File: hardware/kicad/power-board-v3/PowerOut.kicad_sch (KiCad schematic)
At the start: 10 parts, among them J1 3.3V LoRaWAN, J2 3.3V SWARM, J4 5V, J6 12V

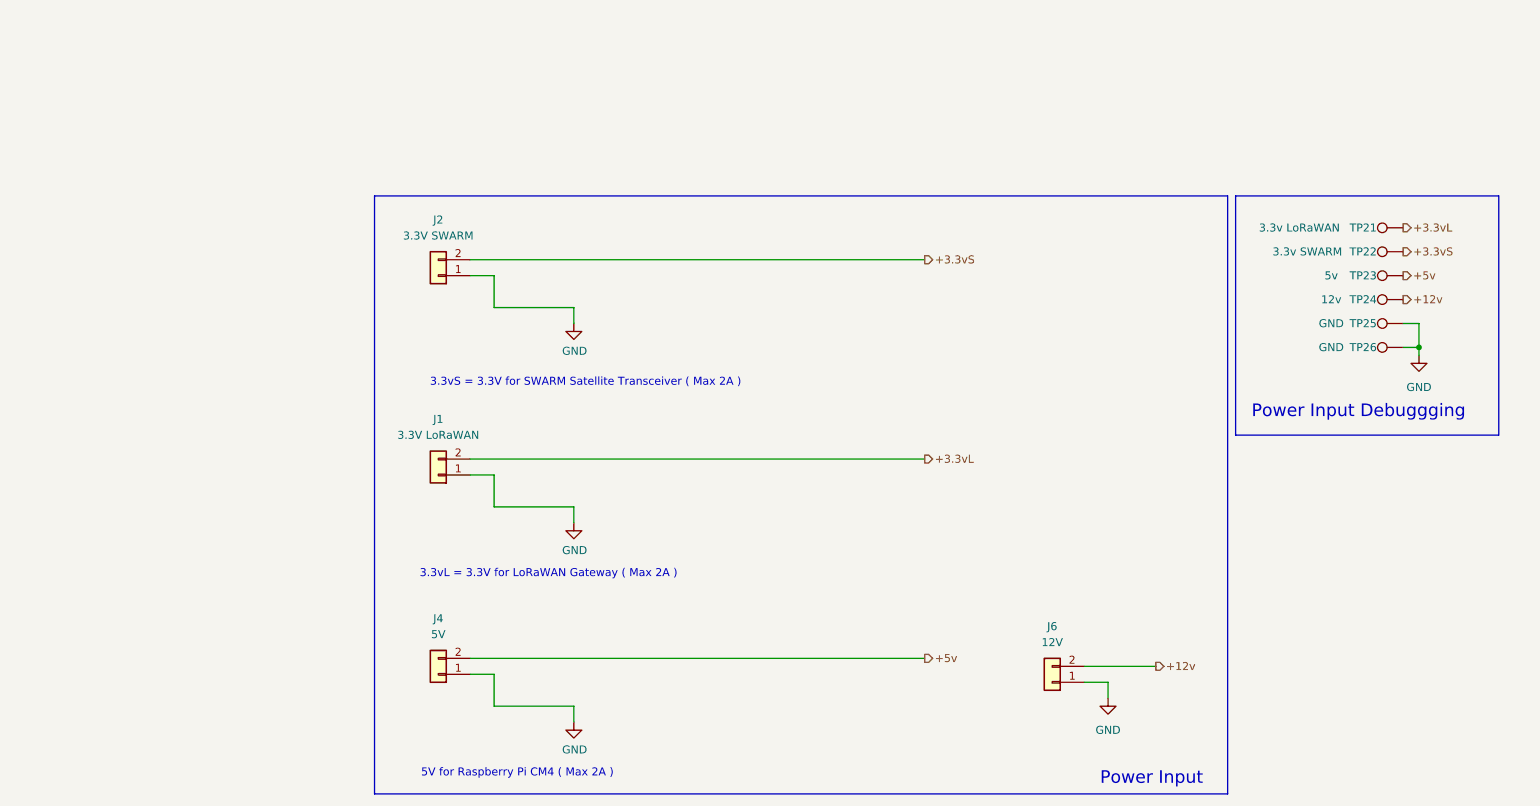
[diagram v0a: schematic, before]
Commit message: add power balance and regulator
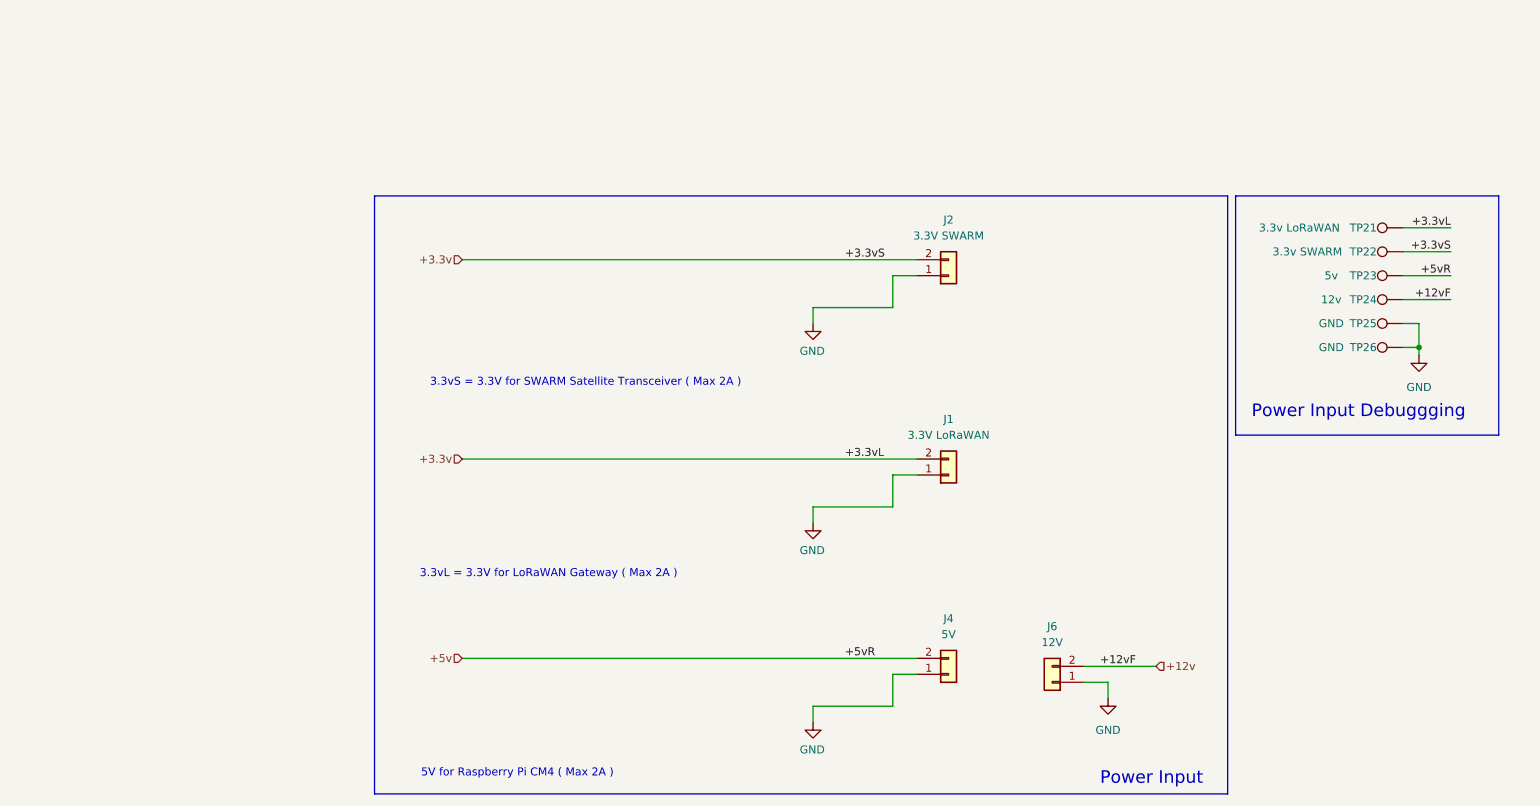
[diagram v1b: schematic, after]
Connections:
- net +3.3vS is gone; now on net +3.3v: J2.2 (Pin_2), TP22.1
- net +3.3vL renamed +3.3v
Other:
- moved on the sheet: J1, J2, J4

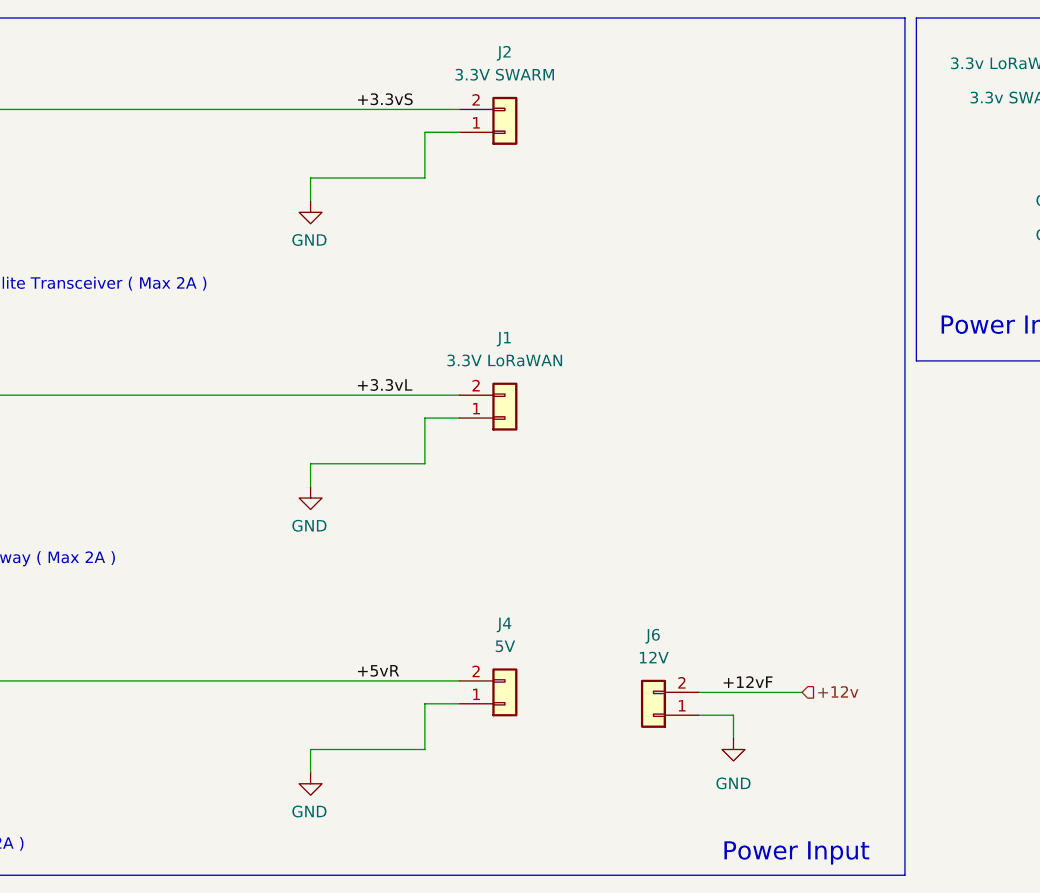
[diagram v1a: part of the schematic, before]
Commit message: add base symbol and wiring
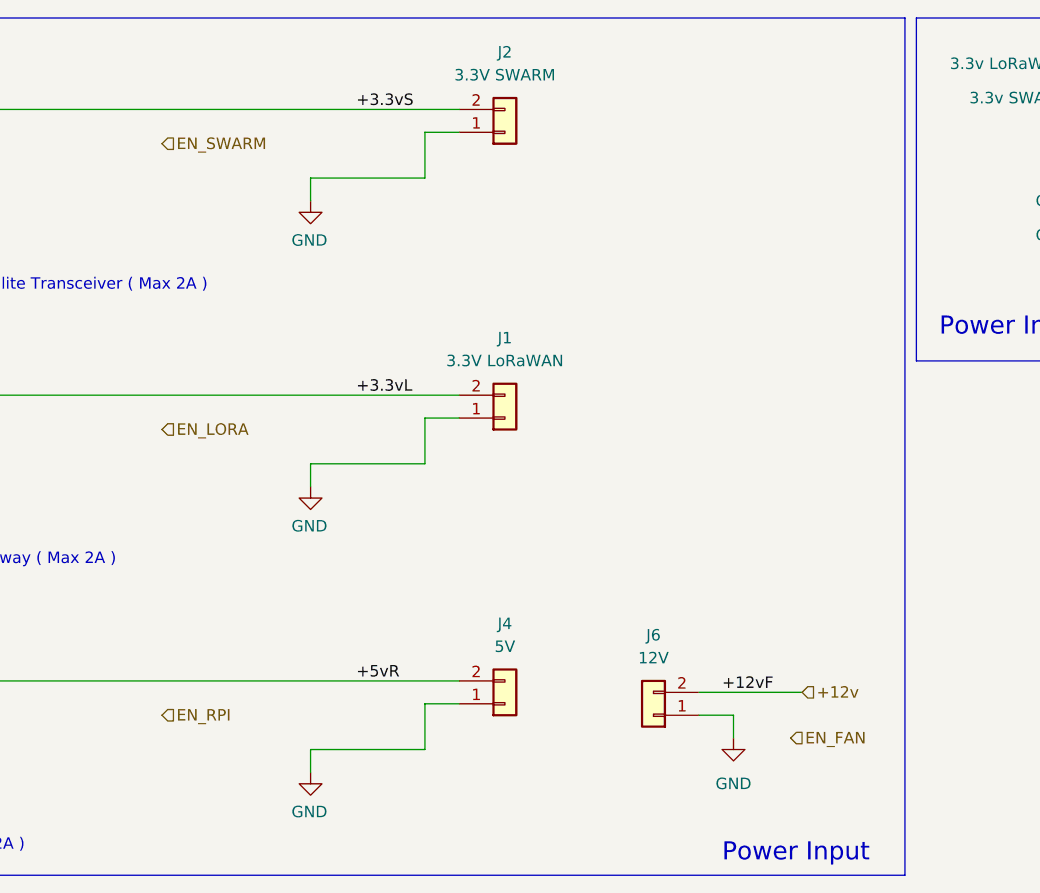
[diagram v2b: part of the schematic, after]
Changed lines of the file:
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@@
     (effects (font (size 1.27 1.27)) (justify right))
+  )
+  (hierarchical_label "EN_FAN" (shape input) (at 196.85 130.81 0)
+    (effects (font (size 1.27 1.27)) (justify left))
+  )
+  (hierarchical_label "EN_RPI" (shape input) (at 127 128.27 0)
+    (effects (font (size 1.27 1.27)) (justify left))
+  )
+  (hierarchical_label "EN_LORA" (shape input) (at 127 96.52 0)
+    (effects (font (size 1.27 1.27)) (justify left))
   )
   (hierarchical_label "+3.3v" (shape input) (at 87.63 92.71 180)
@@
     (effects (font (size 1.27 1.27)) (justify left))
   )
+  (hierarchical_label "EN_SWARM" (shape input) (at 127 64.77 0)
+    (effects (font (size 1.27 1.27)) (justify left))
+  )

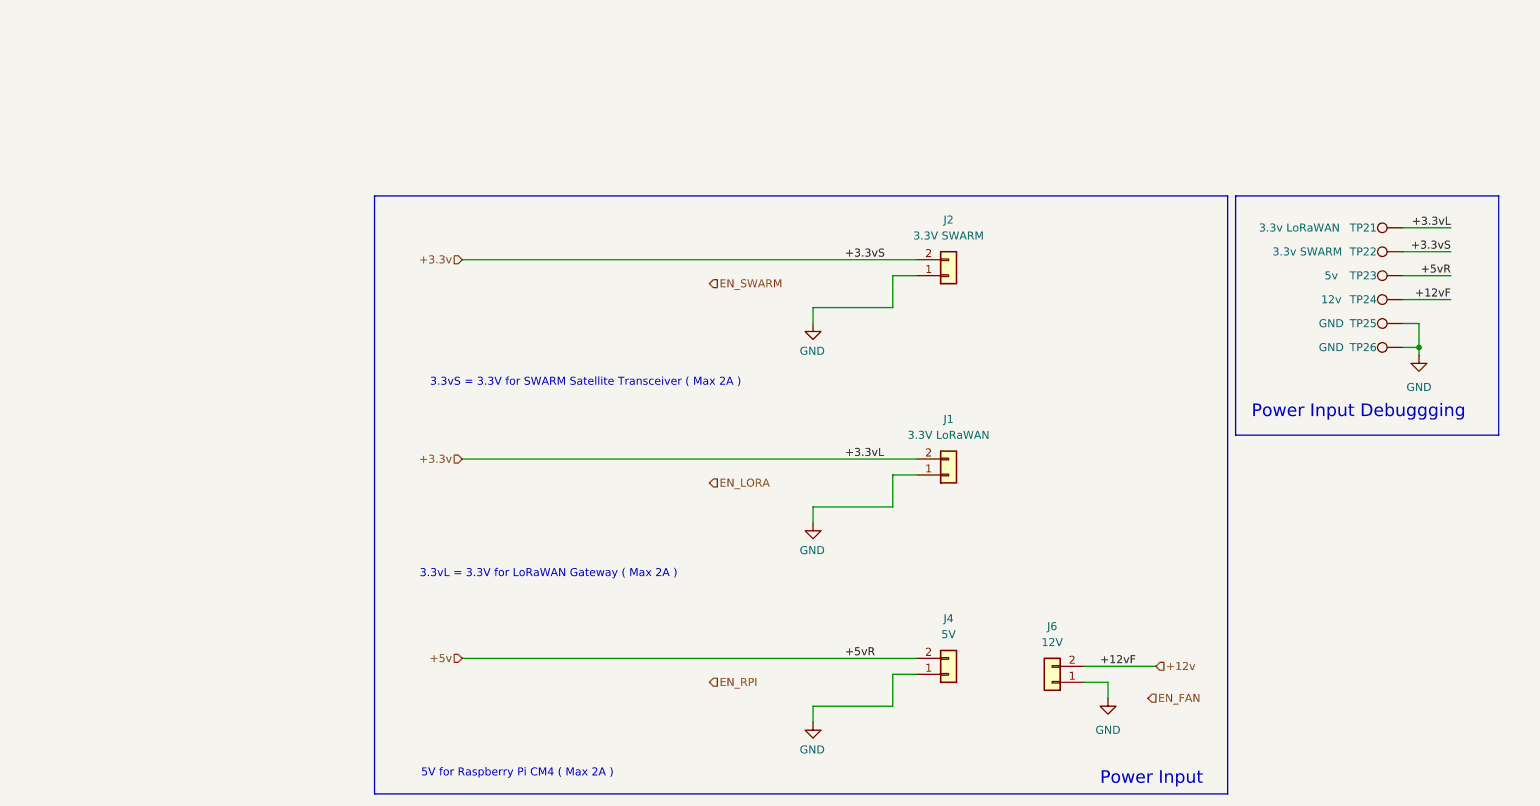
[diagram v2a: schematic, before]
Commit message: initial power switch design
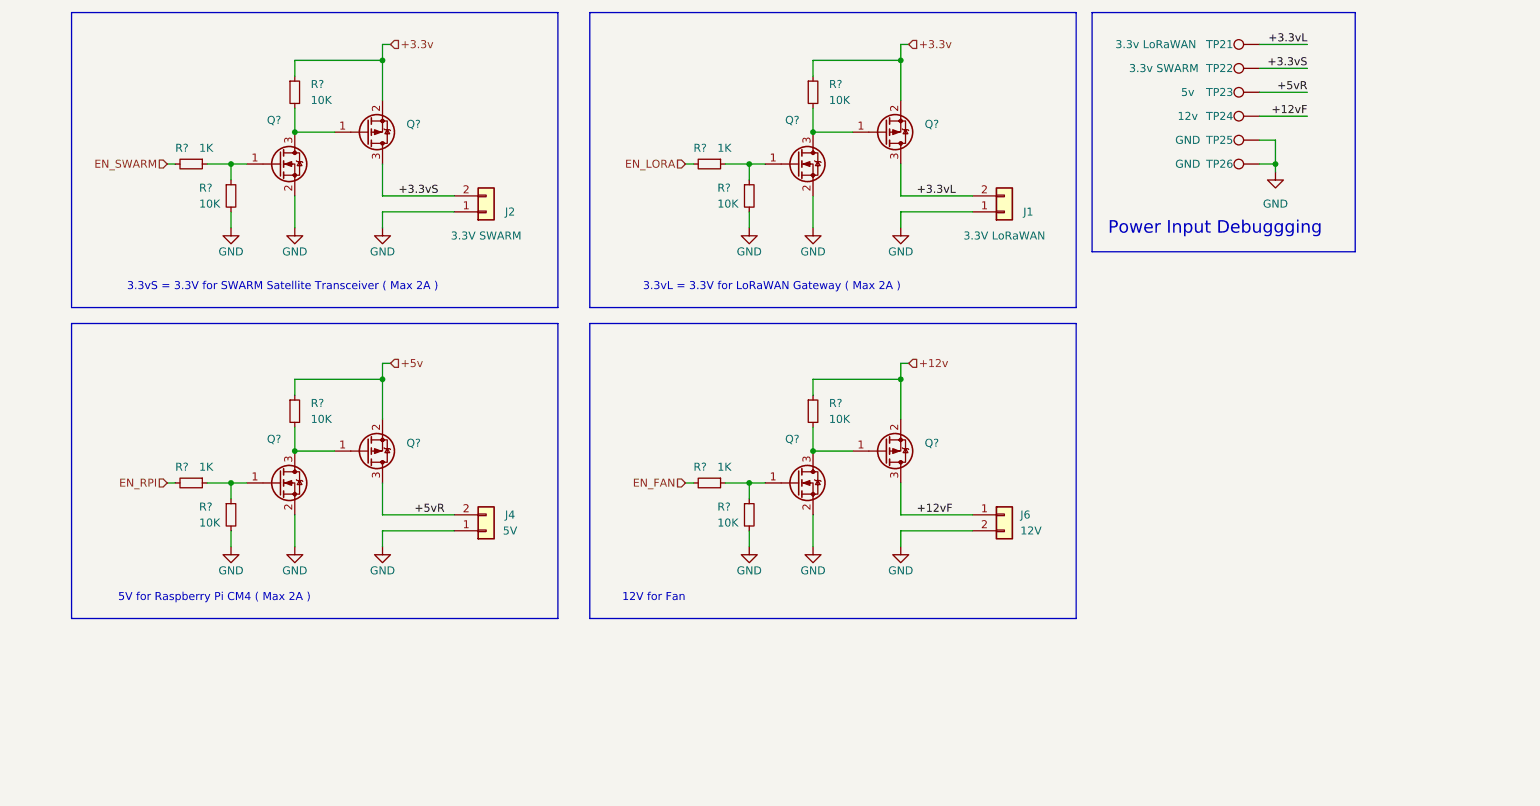
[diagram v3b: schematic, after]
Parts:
- added Q? (x4): ~, Package_TO_SOT_SMD:SOT-23, symbol Device:Q_PMOS_GSD
- added Q? (x4): ~, Package_TO_SOT_SMD:SOT-323_SC-70, symbol Device:Q_NMOS_GSD
- added R? (x8): 10K, Resistor_SMD:R_0603_1608Metric, symbol Device:R_Small
- added R? (x4): 1K, Resistor_SMD:R_0603_1608Metric, symbol Device:R_Small
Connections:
- net +12v: now also Q?.2 (S), R?.1; no longer J6.2 (Pin_2), TP24.1
- net +3.3v: now also Q?.2 (S), Q?.2 (S), R?.1, R?.1; no longer J1.2 (Pin_2), J2.2 (Pin_2), TP21.1, TP22.1
- net +5v: now also Q?.2 (S), R?.1; no longer J4.2 (Pin_2), TP23.1
- net EN_FAN: now also R?.2
- net EN_LORA: now also R?.2
- net EN_RPI: now also R?.2
- net EN_SWARM: now also R?.2
- net GND: now also J6.2 (Pin_2), Q?.2 (S), Q?.2 (S), Q?.2 (S), Q?.2 (S), R?.2, R?.2, R?.2, R?.2; no longer J6.1 (Pin_1)
- new net: Q?.1 (G), R?.1, R?.1 (x4)
- new net: Q?.1 (G), Q?.3 (D), R?.2 (x4)
- new net +12vF: J6.1 (Pin_1), Q?.3 (D), TP24.1
- new net +3.3vL: J1.2 (Pin_2), Q?.3 (D), TP21.1
- new net +3.3vS: J2.2 (Pin_2), Q?.3 (D), TP22.1
- new net +5vR: J4.2 (Pin_2), Q?.3 (D), TP23.1
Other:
- note added: "12V for Fan"
- note removed: "Power Input"
- moved on the sheet: J1, J2, J4, J6, TP21, TP22, TP23, TP24, TP25, TP26
